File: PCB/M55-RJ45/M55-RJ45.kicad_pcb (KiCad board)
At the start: 2 copper layers, 34 x 27.5 mm, 4 parts, among them J1 RJ45, J2 M55 Archer

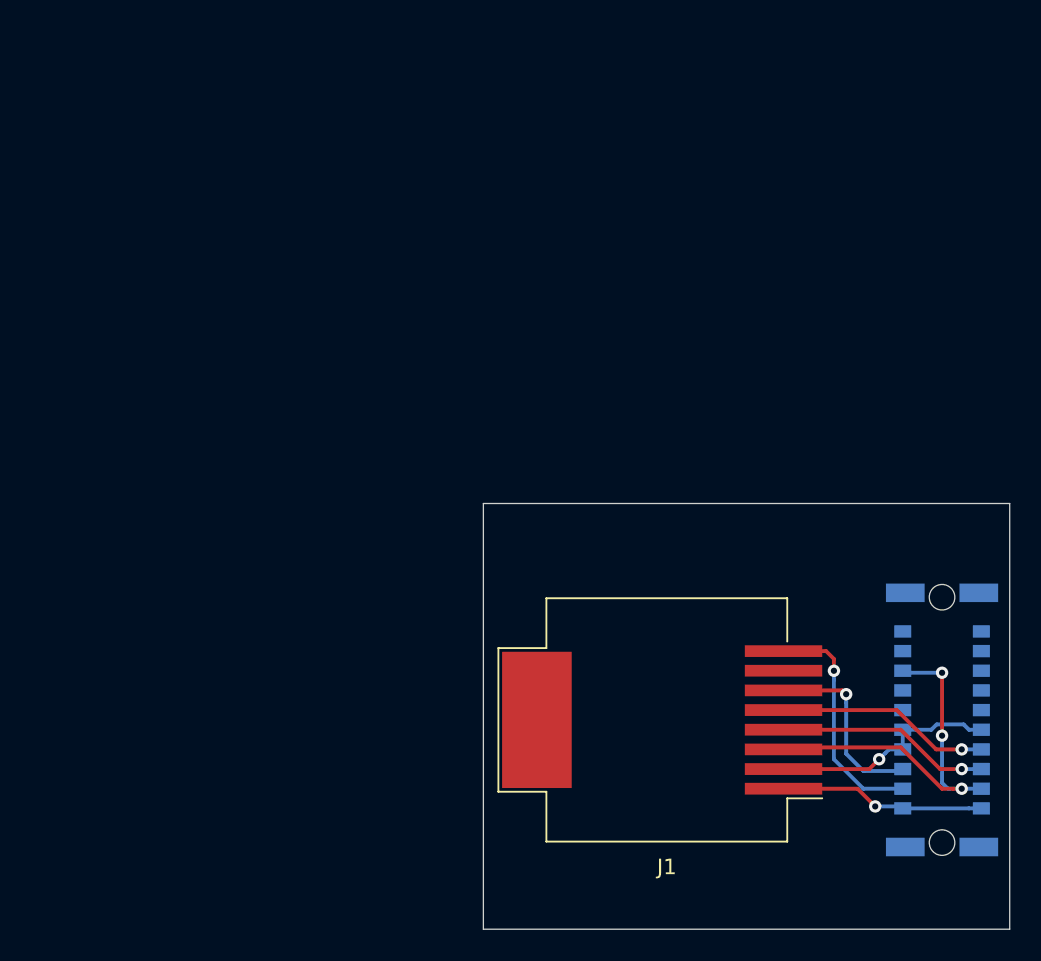
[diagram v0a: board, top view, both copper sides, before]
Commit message: two sided layout
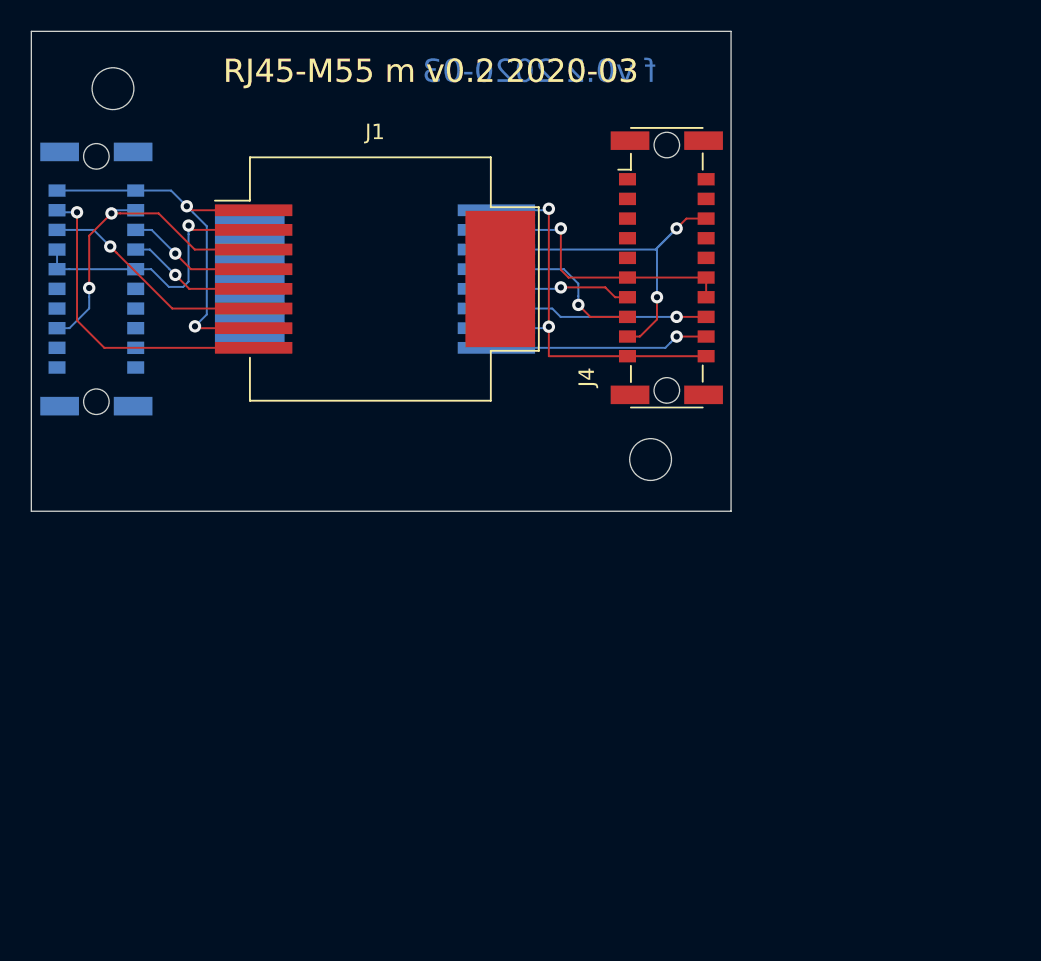
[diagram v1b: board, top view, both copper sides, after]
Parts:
- removed the REF** at (87.4, 169.2)
- removed the REF** at (87.1, 145.5)
- added J3: RJ45, connectors:RJ45_Molex_0855135013_Vertical, B.Cu at (51.0, 129.0)
- added J4: M55 Archer female, connectors:M55-6XX2042R_Archer_Kontrol, F.Cu at (69.8, 128.3)
- added REF**: MountingHole_2.7mm, MountingHole:MountingHole_2.7mm, F.Cu at (68.8, 140.7)
- added REF**: MountingHole_2.7mm, MountingHole:MountingHole_2.7mm, F.Cu at (34.1, 116.7)
- J2: value M55 Archer -> M55 Archer male; footprint connectors:M55-6XX2042R_Archer_Kontrol -> connectors:M55-7XX2042R_Archer_Kontrol
- moved J2 61.6 mm to (33.0, 129.0)
- moved J1 34.2 mm to (51.0, 129.0), turned to 0 degrees
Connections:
- net 5V renamed 5V_m
- net CS0 renamed CS0_m
- net CS1 renamed CS123_m
- net GND renamed GND_m
- net MISO1 renamed MISO1_m
- net MOSI renamed MOSI_m
- net SCK renamed SCK_m
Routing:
- net 5V_f: track 0.00 -> 26.5 mm, vias 0 -> 2
- net GND_f: track 0.00 -> 23.1 mm, vias 0 -> 2
- net CS123_f: track 0.00 -> 17.7 mm, vias 0 -> 1
- net SCK_f: track 0.00 -> 13.9 mm, vias 0 -> 1
- net MISO1_f: track 0.00 -> 13.8 mm, vias 0 -> 1
- net 5V_m: track 13.3 -> 25.8 mm, vias 1 -> 2
- net MOSI_f: track 0.00 -> 10.5 mm, vias 0 -> 1
- net CS0_f: track 0.00 -> 8.77 mm, vias 0 -> 1
- net SCK_m: track 15.2 -> 20.6 mm
- net MOSI_m: track 13.8 -> 8.67 mm
- net CS0_m: track 13.8 -> 8.83 mm
- net GND_m: track 25.1 -> 21.1 mm, vias 3 -> 2
- net CS123_m: track 14.9 -> 18.3 mm
- net MISO1_m: track 12.2 -> 14.8 mm
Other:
- board size 34 x 27.5 mm -> 45.2 x 31 mm
- net class Default: clearance 0.2 -> 0.25
- rule trace_clearance: 0.2 -> 0.25
- board text added: "RJ45-M55 m v0.2 2020-03"
- board text added: "f v0.2 2020-03"
- board text removed: "RJ45-M55 female"
- board text removed: "v0.1"

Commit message: two-sided draft
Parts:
- removed the REF** at (68.8, 140.7)
- removed the REF** at (34.1, 116.7)
- added REF**: MountingHole_2.5x4mm_Pad_VIA, connectors:Mount_via, F.Cu at (43.7, 145.2)
- added REF**: MountingHole_2.5x4mm_Pad_VIA, connectors:Mount_via, F.Cu at (67.8, 140.3)
- moved J2 29.1 mm to (55.7, 147.2), turned to 180 degrees
- moved J1 4.68 mm to (55.7, 129.2), turned to 90 degrees
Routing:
- added copper zone on B.Cu, net (none)
- added copper zone on F.Cu, net (none)
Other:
- board size 45.2 x 31 mm -> 34 x 33.3 mm
- rule trace_min: 0.2 -> 0.127
- board text added: "2020-03"
- board text added: "RJ45-M55 f v0.3"
- board text added: "f"
- board text added: "m"
- board text added: "m v0.3 2020-03"
- board text removed: "RJ45-M55 m v0.2 2020-03"
- board text removed: "f v0.2 2020-03"
